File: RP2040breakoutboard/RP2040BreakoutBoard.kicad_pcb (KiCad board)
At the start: 2 copper layers, 36 parts, among them J1 Conn_02x18_Odd_Even, J2 Conn_02x18_Odd_Even, J3 USB_C_Receptacle_USB2.0_14P, J4 Conn_01x02, U1 RP2040, U2 NCP1117-3.3_SOT223, U3 W25Q128JVS, X1 ABM8-272-T3

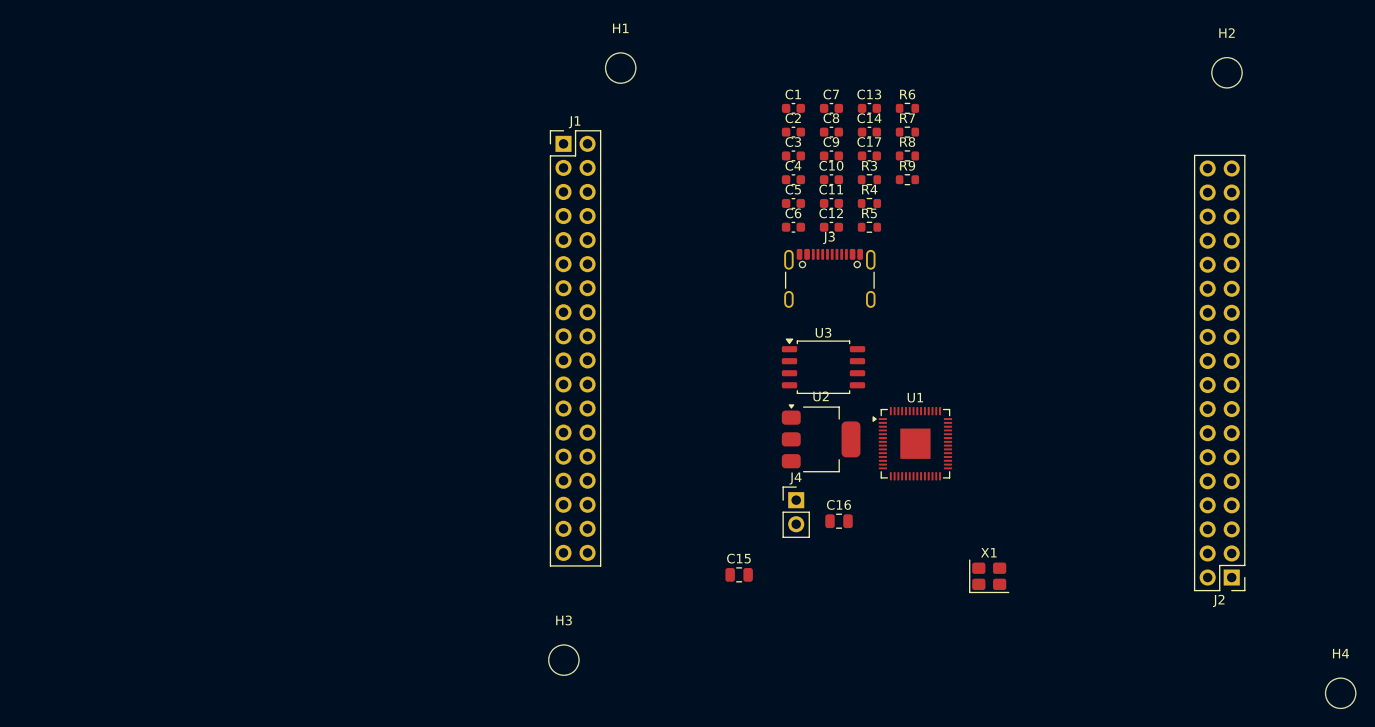
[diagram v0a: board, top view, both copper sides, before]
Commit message: Finished Component Placing
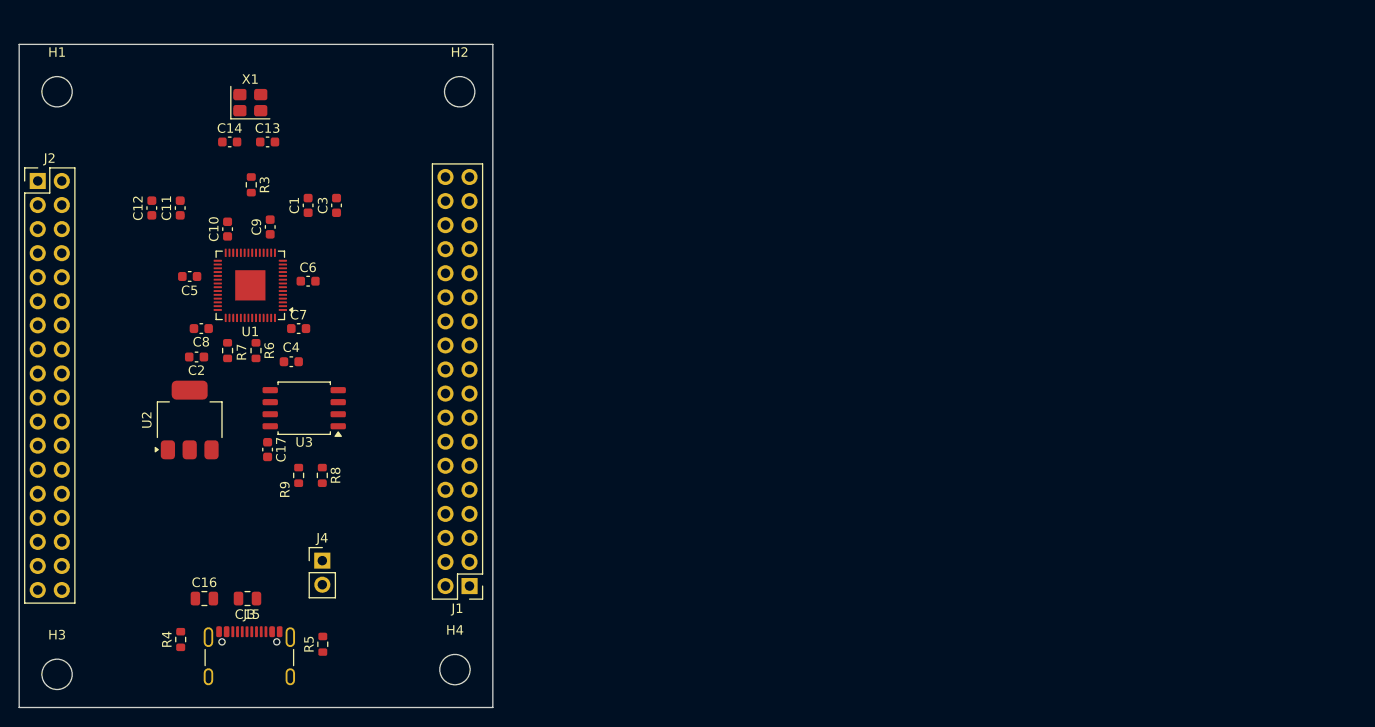
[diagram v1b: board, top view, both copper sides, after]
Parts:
- moved J2 132.8 mm to (70.5, 73.4), turned to 0 degrees
- moved H4 93.5 mm to (114.5, 125.0)
- moved X1 92.6 mm to (92.9, 65.2)
- moved R4 86.1 mm to (85.5, 121.8), turned to 90 degrees
- moved H2 81.0 mm to (115.0, 64.0)
- moved R7 75.4 mm to (90.5, 91.3), turned to -90 degrees
- moved R6 73.4 mm to (93.5, 91.3), turned to -90 degrees
- moved J3 73.1 mm to (92.8, 124.7)
- moved R5 72.6 mm to (100.5, 122.3), turned to 90 degrees
- moved U1 72.2 mm to (92.9, 84.4), turned to 180 degrees
- moved C12 71.8 mm to (82.5, 76.3), turned to 90 degrees
- moved R9 71.4 mm to (98.0, 104.5), turned to 90 degrees
- moved C17 70.7 mm to (94.7, 101.8), turned to -90 degrees
- moved R8 70.4 mm to (100.5, 104.5), turned to -90 degrees
- moved C8 69.7 mm to (87.7, 89.0), turned to 180 degrees
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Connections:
- J2 pad 10: /GPIO20 -> /GPIO17
- J2 pad 12: /GPIO21 -> /GPIO18
- J2 pad 14: /GPIO22 -> /GPIO19
- J2 pad 16: /GPIO23 -> /GPIO20
- J2 pad 18: /GPIO24 -> /GPIO21
- J2 pad 2: /GPIO16 -> /RUN
- J2 pad 20: /GPIO25 -> /GPIO22
- J2 pad 22: /GPIO26 -> /GPIO23
- J2 pad 24: /GPIO27 -> /GPIO24
- J2 pad 26: /GPIO28 -> /GPIO25
- J2 pad 28: /GPIO29 -> /GPIO26
- J2 pad 30: /RUN -> /GPIO27
- J2 pad 32: /SWDIO -> /GPIO28
- J2 pad 34: /SWCLK -> /GPIO29
- J2 pad 4: /GPIO17 -> /SWDIO
- J2 pad 6: /GPIO18 -> /SWCLK
- J2 pad 8: /GPIO19 -> /GPIO16
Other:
- board outline added: 50 x 70 mm

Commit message: Routed
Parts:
- removed R3: 1k, Resistor_SMD:R_0603_1608Metric
- removed X1: ABM8-272-T3, Crystal:Crystal_SMD_3225-4Pin_3.2x2.5mm
- added Y2: Crystal_GND24, Crystal:Crystal_SMD_3225-4Pin_3.2x2.5mm, F.Cu at (93.5, 75.3)
- moved C9 24.3 mm to (96.2, 102.5), turned to -90 degrees
- moved C12 21.1 mm to (93.8, 94.1), turned to -90 degrees
- moved C1 20.3 mm to (88.4, 93.3), turned to 180 degrees
- moved C11 18.8 mm to (88.5, 94.8), turned to 180 degrees
- moved C3 13.3 mm to (88.8, 75.4)
- moved C7 8.49 mm to (104.2, 94.8), turned to -90 degrees
- moved C16 8.01 mm to (85.8, 109.8), turned to 90 degrees
- moved R9 7.95 mm to (102.7, 98.1)
- moved R8 7.39 mm to (104.2, 98.1)
- moved C6 7.10 mm to (105.1, 87.6)
- moved R5 6.54 mm to (95.4, 118.3), turned to -90 degrees
- moved C13 6.34 mm to (96.5, 75.4), turned to -90 degrees
- moved C14 6.18 mm to (90.6, 75.5), turned to 90 degrees
- moved R4 6.12 mm to (90.6, 118.4)
- moved C4 5.94 mm to (102.7, 94.8), turned to -90 degrees
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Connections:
- net /USB_DM renamed /USB_N
- net /USB_DP renamed /USB_P
- C11 pad 2: Net-(C11-Pad2) -> GND
- C12 pad 2: Net-(C11-Pad2) -> GND
- C13 pad 2: GND -> /XIN
- C14 pad 1: GND -> /XOUT
- J2 pad 2: /RUN -> /SWCLK
- J2 pad 6: /SWCLK -> /RUN
- U1 pad 20: GND -> /XIN
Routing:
- net +3V3: track 0.00 -> 105.8 mm
- net /GPIO0: track 0.00 -> 35.7 mm
- net /GPIO29: track 0.00 -> 34.9 mm
- net /GPIO1: track 0.00 -> 34.3 mm
- net /GPIO2: track 0.00 -> 33.4 mm
- net /GPIO28: track 0.00 -> 33.0 mm
- net /GPIO3: track 0.00 -> 32.5 mm
- net Net-(J3-D--PadA7): track 0.00 -> 32.0 mm
- net /GPIO27: track 0.00 -> 30.7 mm
- net /GPIO4: track 0.00 -> 30.3 mm
- net Net-(J3-D+-PadA6): track 0.00 -> 29.6 mm
- net /GPIO26: track 0.00 -> 29.0 mm
- net /GPIO5: track 0.00 -> 27.9 mm
- net /GPIO25: track 0.00 -> 27.0 mm
- net /GPIO24: track 0.00 -> 25.8 mm
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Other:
- board size 50 x 70 mm -> 49.5 x 65.9 mm
